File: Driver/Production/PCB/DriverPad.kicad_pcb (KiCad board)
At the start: 2 copper layers, 120 x 85 mm, 19 parts, among them SW1 SW_Push, SW2 SW_Push, SW3 SW_Push, SW4 SW_Push, SW5 SW_Push, SW6 SW_Push, SW7 SW_Push, SW8 SW_Push, U1 MOUDLE-SEEEDUINO-XIAO, U2 ER_OLEDM0.91_1x-I2C

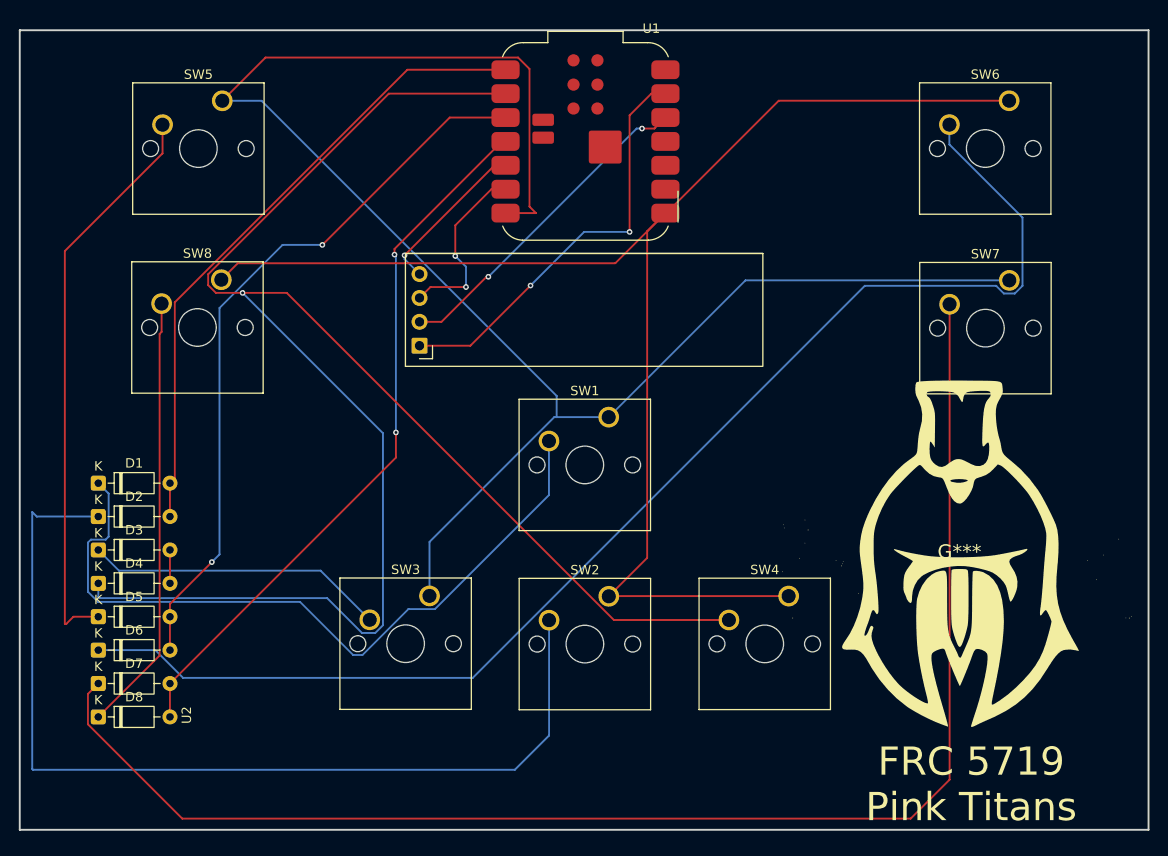
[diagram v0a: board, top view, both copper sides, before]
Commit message: Fixed matrix wiring issues
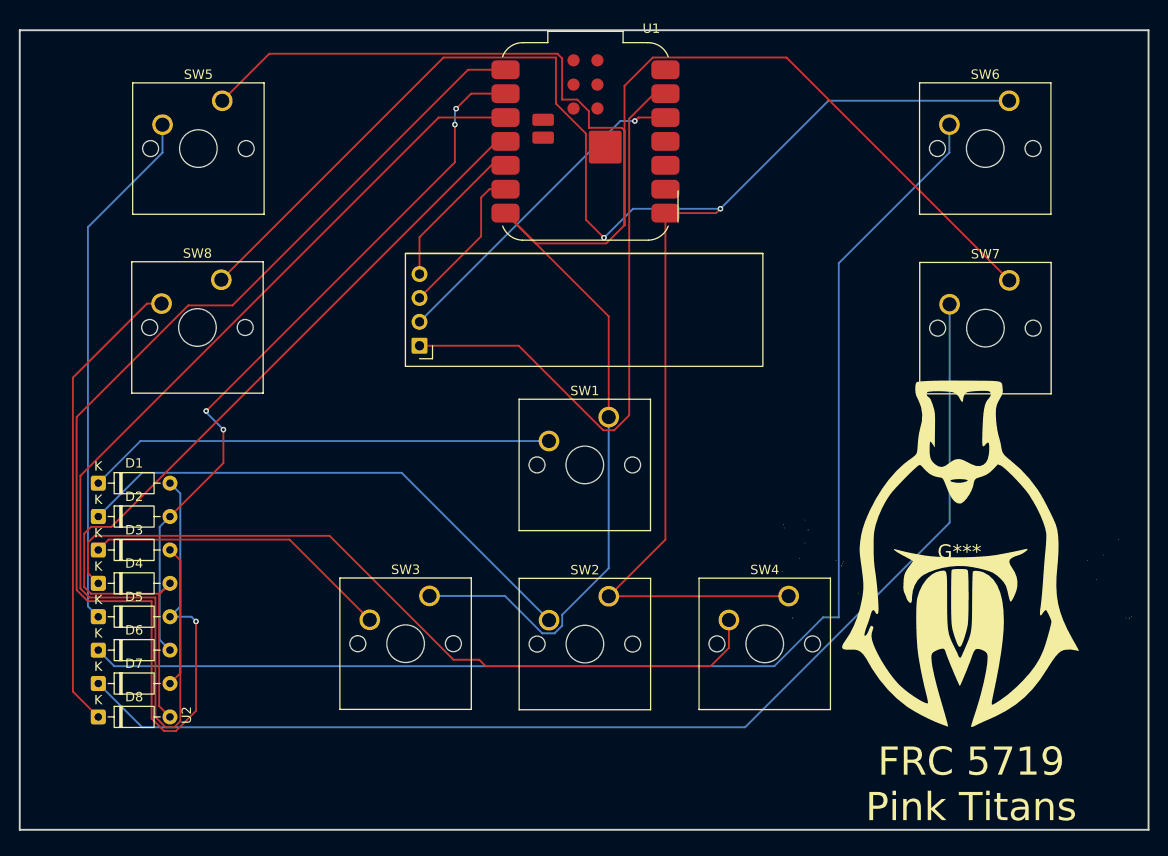
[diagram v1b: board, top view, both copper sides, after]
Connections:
- D2 pad 2: Net-(D1-A) -> Net-(D2-A)
- D4 pad 2: Net-(D3-A) -> Net-(D4-A)
- D5 pad 2: Net-(D5-A) -> Net-(D1-A)
- D6 pad 2: Net-(D5-A) -> Net-(D2-A)
- D7 pad 2: Net-(D7-A) -> Net-(D3-A)
- D8 pad 2: Net-(D7-A) -> Net-(D4-A)
- U1 pad 2: Net-(D4-K) -> Net-(D2-A)
- U1 pad 3: Net-(D5-A) -> Net-(D3-A)
- U1 pad 4: Net-(D7-A) -> Net-(D4-A)
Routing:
- net Net-(D3-A): track 3.55 -> 129.6 mm
- net Net-(D4-K): track 186.0 -> 82.7 mm, vias 1 -> 0
- net Net-(D4-A): track 0.00 -> 92.8 mm
- net Net-(D2-A): track 0.00 -> 78.5 mm, vias 0 -> 4
- net Net-(D5-A): track 77.4 -> 0.00 mm, vias 2 -> 0
- net Net-(D7-A): track 76.3 -> 0.00 mm, vias 2 -> 0
- net Net-(D1-A): track 68.4 -> 134.0 mm, vias 0 -> 1
- net Net-(D2-K): track 103.3 -> 56.3 mm
- net Net-(U1-PB09_A7_D7_RX): track 154.0 -> 184.1 mm, vias 0 -> 2
- net Net-(D1-K): track 78.4 -> 49.8 mm
- net Net-(D7-K): track 152.8 -> 124.7 mm
- net Net-(U1-PB08_A6_D6_TX): track 183.6 -> 210.0 mm
- net Net-(U1-GND): track 44.5 -> 63.2 mm, vias 2 -> 0
- net Net-(D5-K): track 61.2 -> 56.1 mm
- net Net-(D8-K): track 46.7 -> 49.9 mm
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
